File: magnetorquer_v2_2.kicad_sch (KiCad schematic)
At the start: 13 parts, among them U1 MSP430FR5994IPN, Y1 Crystal

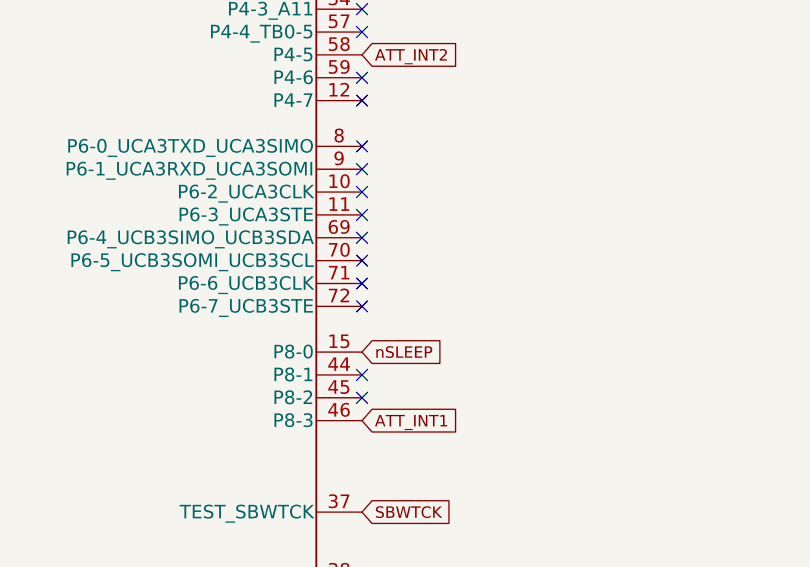
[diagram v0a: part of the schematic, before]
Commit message: added coils
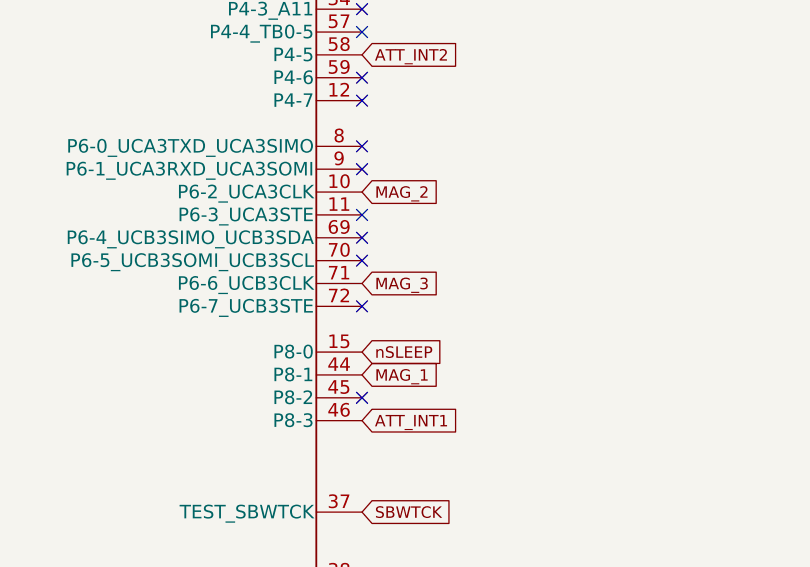
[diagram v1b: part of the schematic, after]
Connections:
- net MAG_2: now reaches U1.10 (P6-2_UCA3CLK)
- net MAG_1: now reaches U1.44 (P8-1)
- net MAG_3: now reaches U1.71 (P6-6_UCB3CLK)
- no-connect marks 54 -> 51
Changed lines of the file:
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@@
   (no_connect (at 226.695 131.445))
   (no_connect (at 226.695 100.965))
-  (no_connect (at 226.695 98.425))
   (no_connect (at 226.695 45.085))
   (no_connect (at 226.695 37.465))
@@
   (no_connect (at 226.695 32.385))
   (no_connect (at 226.695 90.805))
-  (no_connect (at 226.695 88.265))
   (no_connect (at 226.695 85.725))
   (no_connect (at 226.695 83.185))
   (no_connect (at 226.695 80.645))
-  (no_connect (at 226.695 78.105))
   (no_connect (at 226.695 75.565))
   (no_connect (at 226.695 73.025))
@@
     )
   )
+  (global_label "MAG_3" (shape input) (at 226.695 88.265 0) (fields_autoplaced)
+    (effects (font (size 1.27 1.27)) (justify left))
+    (property "Intersheet References" "${INTERSHEET_REFS}" (id 0) (at 235.0952 88.3444 0)
+      (effects (font (size 1.27 1.27)) (justify left) hide)
+    )
+  )
+  (global_label "MAG_2" (shape input) (at 226.695 78.105 0) (fields_autoplaced)
+    (effects (font (size 1.27 1.27)) (justify left))
+    (property "Intersheet References" "${INTERSHEET_REFS}" (id 0) (at 235.0952 78.0256 0)
+      (effects (font (size 1.27 1.27)) (justify left) hide)
+    )
+  )
   (global_label "ATT_CS" (shape input) (at 53.975 100.965 180) (fields_autoplaced)
     (effects (font (size 1.27 1.27)) (justify right))
@@
     (property "Intersheet References" "${INTERSHEET_REFS}" (id 0) (at 44.9095 108.6644 0)
       (effects (font (size 1.27 1.27)) (justify right) hide)
+    )
+  )
+  (global_label "MAG_1" (shape input) (at 226.695 98.425 0) (fields_autoplaced)
+    (effects (font (size 1.27 1.27)) (justify left))
+    (property "Intersheet References" "${INTERSHEET_REFS}" (id 0) (at 235.0952 98.3456 0)
+      (effects (font (size 1.27 1.27)) (justify left) hide)
     )
   )
@@
       (reference "#PWR016") (unit 1) (value "+5V") (footprint "")
     )
+    (path "/8c105609-fc66-44c7-9dd5-b8497277d331/fd6019ec-3727-4b1f-8596-67f4ed2f93dc"
+      (reference "#PWR017") (unit 1) (value "+3V3") (footprint "")
+    )
+    (path "/8c105609-fc66-44c7-9dd5-b8497277d331/c483868f-9b27-4813-812a-2434f2e5d4f4"
+      (reference "#PWR018") (unit 1) (value "GND") (footprint "")
+    )
+    (path "/8c105609-fc66-44c7-9dd5-b8497277d331/46495172-ff36-45ff-9d79-77c34de456dd"
+      (reference "#PWR019") (unit 1) (value "+3V3") (footprint "")
+    )
+    (path "/8c105609-fc66-44c7-9dd5-b8497277d331/b845f0fb-2c2a-4ec9-a67b-b48fc3d8e8a6"
+      (reference "#PWR020") (unit 1) (value "GND") (footprint "")
+    )
+    (path "/8c105609-fc66-44c7-9dd5-b8497277d331/c53d3807-4728-4171-a28e-9a97edcc1b18"
+      (reference "#PWR021") (unit 1) (value "+3V3") (footprint "")
+    )
+    (path "/8c105609-fc66-44c7-9dd5-b8497277d331/181540bc-298e-4af4-8819-be8bafd4cdb0"
+      (reference "#PWR022") (unit 1) (value "GND") (footprint "")
+    )
     (path "/71d4ddb6-f6ba-4a29-9139-44d5a4622a71/a8a1e016-4829-4884-85b1-82c5d2156566"
       (reference "#PWR0101") (unit 1) (value "GND") (footprint "")
@@
       (reference "D2") (unit 1) (value "LED_GREEN") (footprint "LED_SMD:LED_0805_2012Metric")
     )
+    (path "/8c105609-fc66-44c7-9dd5-b8497277d331/1746181e-508d-4e4c-b918-ececc99985a2"
+      (reference "IC1") (unit 1) (value "AH9247Z3-G1") (footprint "Package_TO_SOT_THT:TO-92Flat")
+    )
+    (path "/8c105609-fc66-44c7-9dd5-b8497277d331/72f1e5af-bec4-41f1-9edd-2323c93eeea2"
+      (reference "IC2") (unit 1) (value "AH9247Z3-G1") (footprint "Package_TO_SOT_THT:TO-92Flat")
+    )
+    (path "/8c105609-fc66-44c7-9dd5-b8497277d331/53faa66c-26db-4270-9702-ee5038c3f89d"
+      (reference "IC3") (unit 1) (value "AH9247Z3-G1") (footprint "Package_TO_SOT_THT:TO-92Flat")
+    )
     (path "/71d4ddb6-f6ba-4a29-9139-44d5a4622a71/d0cb625f-2309-4336-9dbb-f4690cb2cc25"

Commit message: new uc
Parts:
- removed U1: MSP430FR5994IPN, magnetorquer:MSP430FR5994IPN, symbol MSP430FR5994IPN:MSP430FR5994IPN
- added R3, R4, R5, R6: 0R, Resistor_SMD:R_0805_2012Metric, symbol Device:R
- added U1: MSP430FR6972IPM, magnetorquer:MSP430FR6972IPM, symbol MSP430FR6972IPM-B:MSP430FR6972IPM
- C3: footprint Capacitor_SMD:C_0805_2012Metric -> Capacitor_Tantalum_SMD:CP_EIA-3216-18_Kemet-A
- D1, D2: footprint LED_SMD:LED_0805_2012Metric -> LED_SMD:LED_0603_1608Metric
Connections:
- net +3V3: now also U1.18 (DVCC1), U1.40 (DVCC2), U1.49 (AVCC1), U1.63 (DVCC3)
- net ATT_CS: now also U1.30 (P2-3_UCA0STE_TB0OUTH_S19)
- net ATT_INT1: now also U1.35 (P7-1_TA0-0_S14)
- net ATT_INT2: now also U1.34 (P7-0_TA0CLK_S15)
- net ATT_SCL: now also U1.31 (P2-2_UCA0CLK_TB0-4_RTCCLK_S18)
- net ATT_SDI: now also U1.33 (P2-0_UCA0SIMO_UCA0TXD_TB0-6_TB0CLK_S16)
- net ATT_SDO: now also U1.32 (P2-1_UCA0SOMI_UCA0RXD_TB0-5_DMAE0_S17)
- net BCLUART_RXD: now also U1.1 (P4-3_UCA0SOMI_UCA0RXD_UCB1STE_S4)
- net BCLUART_TXD: now also U1.64 (P4-2_UCA0SIMO_UCA0TXD_UCB1CLK_S5)
- net GND: now also U1.17 (DVSS1), U1.39 (DVSS2), U1.50 (AVSS1), U1.53 (AVSS2), U1.56 (AVSS3), U1.62 (DVSS3)
- net H1_IN1: now also U1.36 (P7-2_TA0-1_S13)
- net H1_IN2: now also U1.37 (P7-3_TA0-2_S12)
- net H2_IN1: now also U1.15 (P3-1_UCB1SIMO_UCB1SDA_TA3-3_S26)
- net H2_IN2: now also U1.14 (P3-0_UCB1CLK_TA3-2_S27)
- net H3_IN1: now also U1.60 (P4-6_UCB1SIMO_UCB1SDA_TA1-1_S7)
- net H3_IN2: now also U1.61 (P4-7_UCB1SOMI_UCB1SCL_TA1-2_S6)
- net MAG_1: now also U1.47 (P9-6_A14_C14)
- net MAG_2: now also U1.46 (P9-5_A13_C13)
- net MAG_3: now also U1.45 (P9-4_A12_C12)
- net SBWTCK: now also U1.19 (TEST_SBWTCK)
- net SBWTDIO: now also U1.20 (RST_NMI_SBWTDIO_N)
- net nSLEEP: now also U1.11 (P6-4_TB0-0_COM1_S30)
- net at R1.1: now also U1.44 (P1-0_TA0-1_DMAE0_RTCCLK_A0_C0_VREF-_VEREF-)
- net at C1.2, Y1.1: now also U1.52 (PJ-5_LFXOUT)
- net at C2.2, Y1.2: now also U1.51 (PJ-4_LFXIN)
- net at R2.1: now also U1.43 (P1-1_TA0-2_TA1CLK_COUT_A1_C1_VREF+_VEREF+)
- new net: R3.2, U1.26 (P3-4_UCA1SIMO_UCA1TXD_TB0-0_S23)
- new net: R4.2, U1.27 (P3-5_UCA1SOMI_UCA1RXD_TB0-1_S22)
- new net: R5.2, U1.28 (P3-6_UCA1CLK_TB0-2_S21)
- new net: R6.2, U1.29 (P3-7_UCA1STE_TB0-3_S20)
- new net SPI-CLK: R5.1
- new net SPI-CS: R6.1
- new net SPI-MISO: R4.1
- new net SPI-MOSI: R3.1
- no-connect marks 51 -> 26
